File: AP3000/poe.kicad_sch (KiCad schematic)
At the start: 89 parts, among them IC2 TPS23751PWPR, J11 Barrel_Jack, Q1 BSC520N15NS3 G, Q2 MMBT2907ALT1G, Q3 MMBT3906LT1G, U10 SIR422DP-T1-GE3, U12 TCMT1107, U13 TLV431ACDBZR

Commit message: Route all the high speed lines and most gpio
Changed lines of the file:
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@@
   (junction (at 271.78 77.47) (diameter 1.016) (color 0 0 0 0))
   (junction (at 271.78 93.98) (diameter 1.016) (color 0 0 0 0))
+  (no_connect (at 125.73 155.575))
   (no_connect (at 115.57 155.575))
-  (no_connect (at 125.73 155.575))
   (no_connect (at 40.64 114.3))
   (wire (pts (xy 15.24 77.47) (xy 26.67 77.47))
@@
     (effects (font (size 1.27 1.27)) (justify right bottom))
   )
-  (label "+5V" (at 265.43 77.47 0)
+  (label "+5v" (at 265.43 77.47 0)
     (effects (font (size 1.27 1.27)) (justify left bottom))
   )
-  (label "+5V" (at 274.32 106.68 0)
+  (label "+5v" (at 274.32 106.68 0)
     (effects (font (size 1.27 1.27)) (justify left bottom))
   )

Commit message: AP3000: Fixup PartsBoxID linkage and placed first order Working on a design for a 5 GHz panel antenna array for a point-to-point replacement
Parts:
- C10, C9: PartsBoxID EEE-FK0J331XP -> EEEFK0J331XP
- C12, C13, C14: PartsBoxID 1206-100uF-X5R-6.3V -> 1206-47uF-X5R-10V
- C29: PartsBoxID EEE-FK1E220R -> EEEFK1E220R
- D17, D18: PartsBoxID (none) -> BAT54SW-7-F
- IC2: PartsBoxID (none) -> TPS23751PWPR
- Q1: PartsBoxID BSC520N15NS3 G -> BSC520N15NS3GATMA1
- U12: PartsBoxID (none) -> TCMT1107
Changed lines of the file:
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@@
       (effects (font (size 1.27 1.27)) hide)
     )
-    (property "PartsBoxID" "1206-100uF-X5R-6.3V" (id 4) (at 212.09 85.09 0)
+    (property "PartsBoxID" "1206-47uF-X5R-10V" (id 4) (at 212.09 85.09 0)
       (effects (font (size 1.27 1.27)) hide)
     )
@@
       (effects (font (size 1.27 1.27)) hide)
     )
-    (property "PartsBoxID" "1206-100uF-X5R-6.3V" (id 4) (at 220.98 85.09 0)
+    (property "PartsBoxID" "1206-47uF-X5R-10V" (id 4) (at 220.98 85.09 0)
       (effects (font (size 1.27 1.27)) hide)
     )
@@
       (effects (font (size 1.27 1.27)) hide)
     )
-    (property "PartsBoxID" "1206-100uF-X5R-6.3V" (id 4) (at 229.87 85.09 0)
+    (property "PartsBoxID" "1206-47uF-X5R-10V" (id 4) (at 229.87 85.09 0)
       (effects (font (size 1.27 1.27)) hide)
     )
@@
       (effects (font (size 1.27 1.27)) (justify left) hide)
     )
-    (property "PartsBoxID" "EEE-FK1E220R" (id 4) (at 116.84 104.14 0)
+    (property "PartsBoxID" "EEEFK1E220R" (id 4) (at 116.84 104.14 0)
       (effects (font (size 1.27 1.27)) hide)
     )
@@
       (effects (font (size 1.27 1.27)) (justify left) hide)
     )
-    (property "PartsBoxID" "EEE-FK0J331XP" (id 4) (at 238.76 78.74 0)
+    (property "PartsBoxID" "EEEFK0J331XP" (id 4) (at 238.76 78.74 0)
       (effects (font (size 1.27 1.27)) hide)
     )
@@
       (effects (font (size 1.27 1.27)) (justify left) hide)
     )
-    (property "PartsBoxID" "EEE-FK0J331XP" (id 4) (at 262.89 78.74 0)
+    (property "PartsBoxID" "EEEFK0J331XP" (id 4) (at 262.89 78.74 0)
       (effects (font (size 1.27 1.27)) hide)
     )
@@
       (effects (font (size 1.27 1.27)) hide)
     )
+    (property "PartsBoxID" "BAT54SW-7-F" (id 4) (at 186.69 137.16 0)
+      (effects (font (size 1.27 1.27)) hide)
+    )
   )
   (symbol (lib_id "Diode:BAT54S") (at 254.635 129.54 270) (mirror x) (unit 1)
@@
       (effects (font (size 1.27 1.27)) hide)
     )
+    (property "PartsBoxID" "BAT54SW-7-F" (id 4) (at 254.635 129.54 0)
+      (effects (font (size 1.27 1.27)) hide)
+    )
   )
   (symbol (lib_id "Isolator:TCMT1107") (at 214.63 139.7 0) (mirror y) (unit 1)
@@
       (effects (font (size 1.27 1.27)) (justify left) hide)
     )
+    (property "PartsBoxID" "TCMT1107" (id 4) (at 214.63 139.7 0)
+      (effects (font (size 1.27 1.27)) hide)
+    )
   )
   (symbol (lib_id "AP3000:TRANSF5") (at 120.65 155.575 180) (unit 1)
@@
       (effects (font (size 1.27 1.27)) (justify left) hide)
     )
-    (property "PartsBoxID" "BSC520N15NS3 G" (id 4) (at 144.78 113.03 0)
+    (property "PartsBoxID" "BSC520N15NS3GATMA1" (id 4) (at 144.78 113.03 0)
       (effects (font (size 1.27 1.27)) hide)
     )
@@
       (effects (font (size 1.27 1.27)) (justify left) hide)
     )
-  )
+    (property "PartsBoxID" "TPS23751PWPR" (id 4) (at 40.64 99.06 0)
+      (effects (font (size 1.27 1.27)) hide)
+    )
+  )

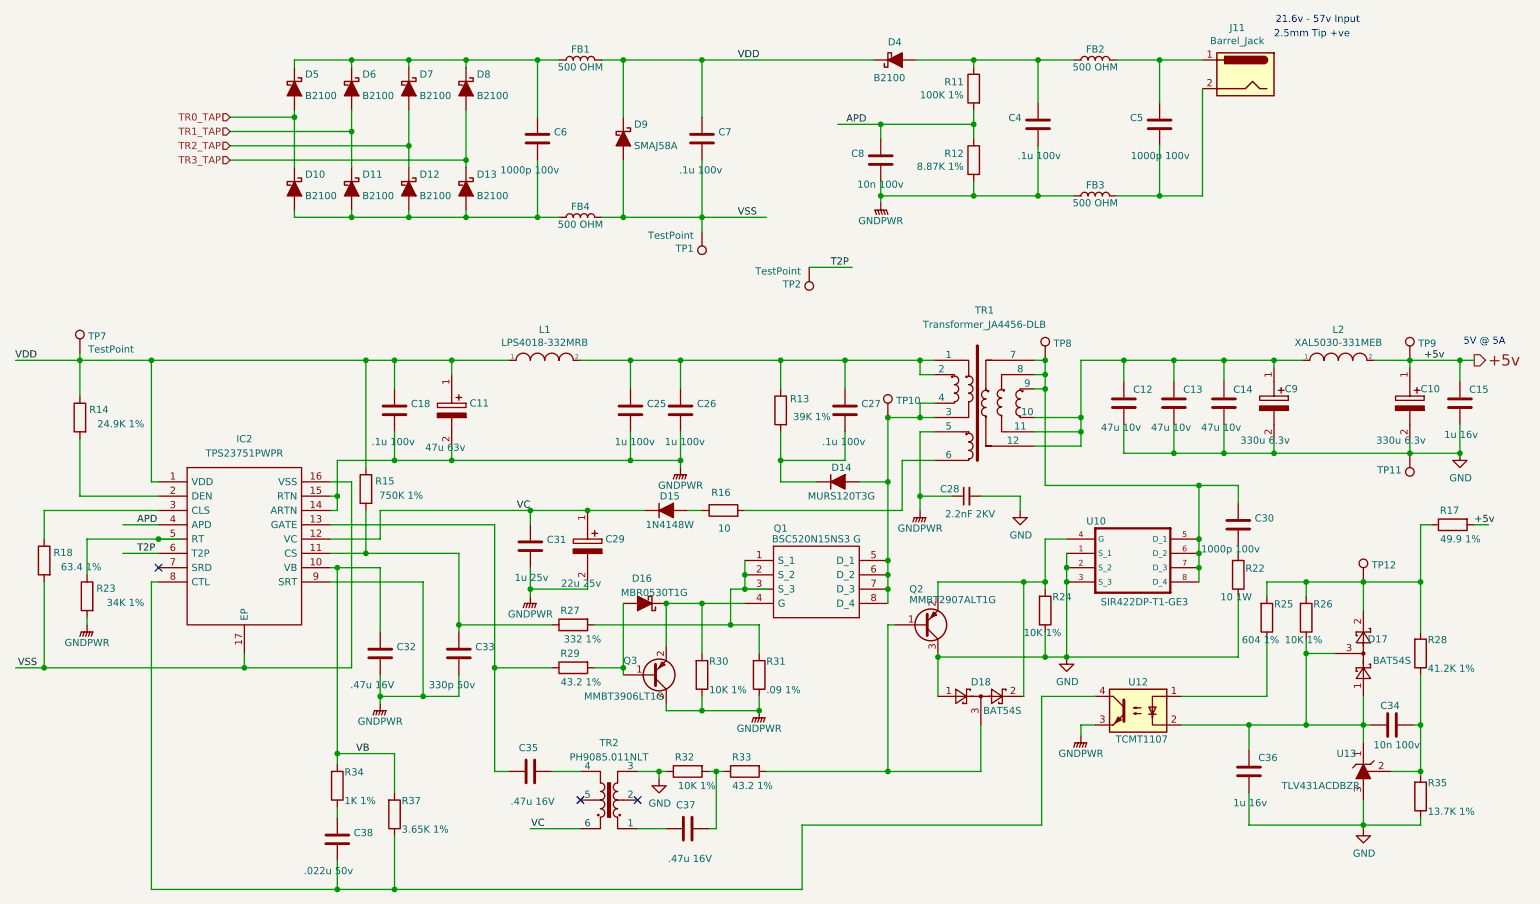
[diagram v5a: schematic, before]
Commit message: Rework AP3000 PoE section, power section and change solder paste to -10% overall, -15% for small chips / mpcie and -20% for the raspi connector
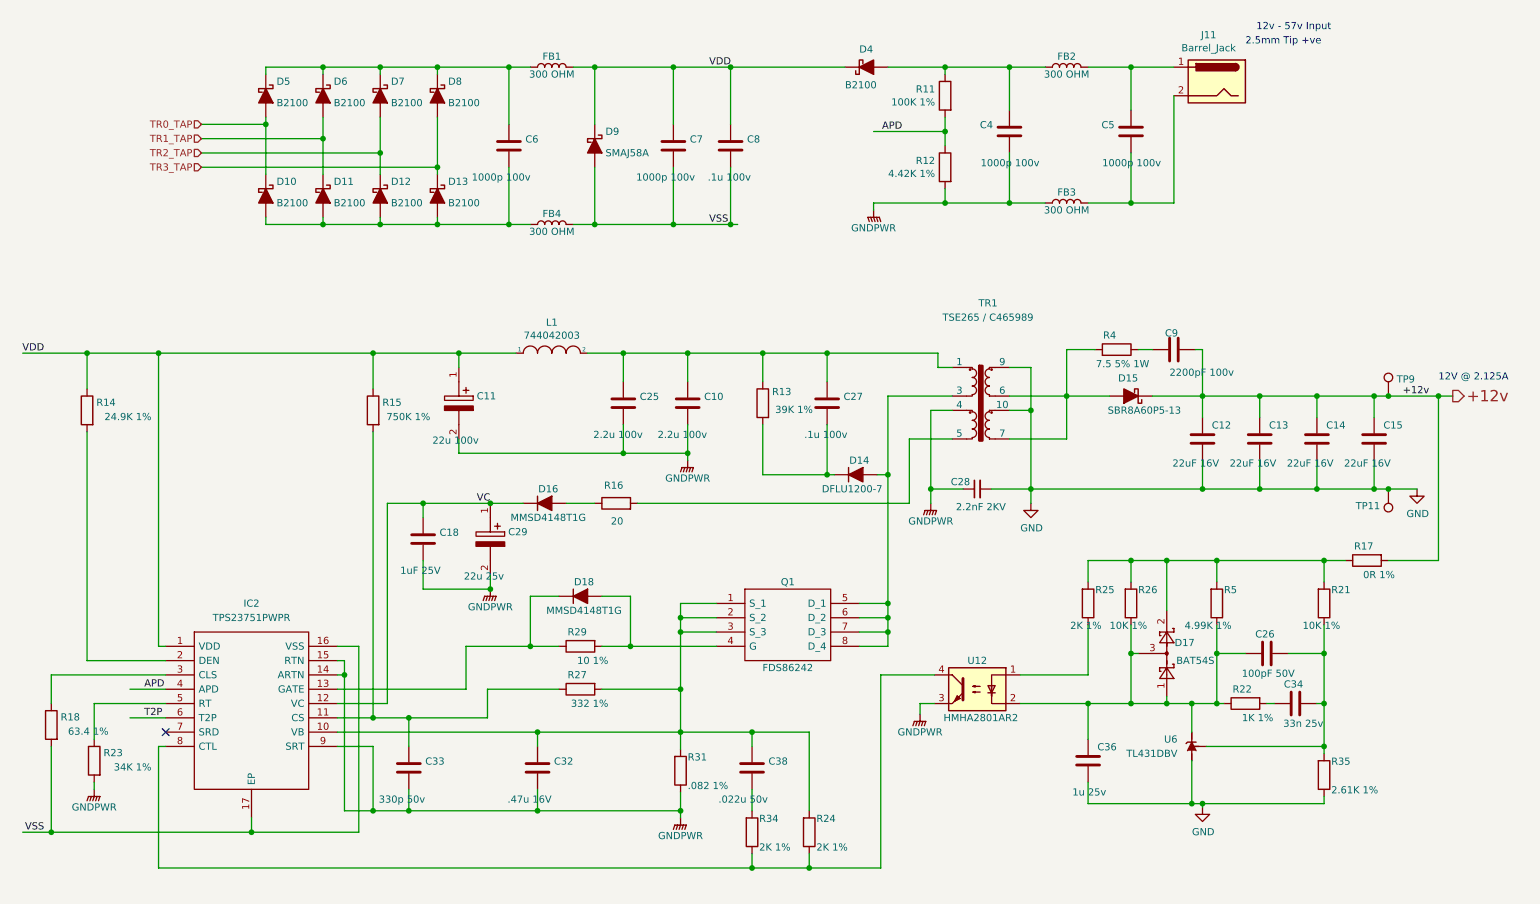
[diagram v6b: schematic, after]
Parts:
- removed C10, C9: 330u 6.3v, Capacitor_SMD:CP_Elec_6.3x7.7, symbol AP3000-rescue:EEEFK2A330P-EEEFK2A330P
- removed C30: 1000p 100v, Capacitor_SMD:C_0805_2012Metric, symbol Device:C
- removed C31: 1u 25v, Capacitor_SMD:C_0805_2012Metric, symbol Device:C
- removed C35, C37: .47u 16V, Capacitor_SMD:C_0603_1608Metric, symbol Device:C
- removed D15: 1N4148W, Diode_SMD:D_SOD-123, symbol Device:D_ALT
- removed D16: MBR0530T1G, Diode_SMD:D_SOD-123, symbol Device:D_Schottky_ALT
- removed D18: BAT54S, Package_TO_SOT_SMD:SOT-23, symbol Diode:BAT54S
- removed L2: XAL5030-331MEB, Inductor_SMD:L_Coilcraft_XAL5030, symbol pspice:INDUCTOR
- removed Q2: MMBT2907ALT1G, Package_TO_SOT_SMD:SOT-23, symbol Device:Q_PNP_BEC
- removed Q3: MMBT3906LT1G, Package_TO_SOT_SMD:SOT-23, symbol Device:Q_PNP_BEC
- removed R28: 41.2K 1%, Resistor_SMD:R_0402_1005Metric, symbol Device:R
- removed R30, R32: 10K 1%, Resistor_SMD:R_0402_1005Metric, symbol Device:R
- removed R33: 43.2 1%, Resistor_SMD:R_0402_1005Metric, symbol Device:R
- removed R37: 3.65K 1%, Resistor_SMD:R_0402_1005Metric, symbol Device:R
- removed TP1, TP10, TP12, TP2, TP7, TP8: TestPoint, TestPoint:TestPoint_Pad_2.0x2.0mm, symbol Connector:TestPoint
- removed TR2: PH9085.011NLT, AP3000:XFMR_PH9085.011NLT, symbol AP3000:TRANSF5
- removed U10: SIR422DP-T1-GE3, Scott:TRANS_STL60P4LLF6, symbol STL90N6F7:STL90N6F7
- removed U13: TLV431ACDBZR, Package_TO_SOT_SMD:SOT-23, symbol dk_PMIC-Voltage-Reference:TL431AIDBZR
- added C10: 2.2u 100v, Capacitor_SMD:C_1210_3225Metric, symbol Device:C
- added C9: 2200pF 100v, Capacitor_SMD:C_0603_1608Metric, symbol Device:C
- added D15: SBR8A60P5-13, Diode_SMD:D_PowerDI-5, symbol Device:D_Schottky_ALT
- added D16, D18: MMSD4148T1G, Diode_SMD:D_SOD-123, symbol Device:D_ALT
- added R21: 10K 1%, Resistor_SMD:R_0603_1608Metric, symbol Device:R
- added R4: 7.5 5% 1W, Resistor_SMD:R_2512_6332Metric, symbol Device:R
- added R5: 4.99K 1%, Resistor_SMD:R_0603_1608Metric, symbol Device:R
- added U6: TL431DBV, Package_TO_SOT_SMD:SOT-23-5, symbol Reference_Voltage:TL431DBV
- C11: value 47u 63v -> 22u 100v; PartsBoxID EEE-FK1J470P -> EEEFK2A220P
- C12, C13, C14: value 47u 10v -> 22uF 16V; footprint Capacitor_SMD:C_1206_3216Metric -> Capacitor_SMD:C_1210_3225Metric; Part Description 47uF 10% or 20% 10V Ceramic Capacitor X5R 1206 -> GCM32ER71C226KE19L; PartsBoxID 1206-47uF-X5R-10V -> 1210-22uF-X7R-16V
- C15: value 1u 16v -> 22uF 16V; footprint Capacitor_SMD:C_0805_2012Metric -> Capacitor_SMD:C_1210_3225Metric; Field4 (none) -> Mouser; Part Description 1uF 10% or 20% 16V Ceramic Capacitor X7R 0805 -> GCM32ER71C226KE19L; PartsBoxID 0805-1uF-X7R-16V -> 1210-22uF-X7R-16V
- C18: value .1u 100v -> 1uF 25V; footprint Capacitor_SMD:C_0603_1608Metric -> Capacitor_SMD:C_0805_2012Metric; Part Description .1uF 10% or 20% 100V Ceramic Capacitor X7R 0603 -> C2012X5R1E105K; PartsBoxID 0603-100nF-X7R-100V -> 0805-1uF-X5R-25V
- C25: value 1u 100v -> 2.2u 100v; footprint Capacitor_SMD:C_1206_3216Metric -> Capacitor_SMD:C_1210_3225Metric; Field7 CL31B105KCHNNNE -> (none); Part Description 1uF 10% or 20% 100V Ceramic Capacitor X7R 1206 -> (none); PartsBoxID 1206-1uF-X7R-100V -> 1210-2.2uF-X7R-100V
- C26: value 1u 100v -> 100pF 50V; footprint Capacitor_SMD:C_1206_3216Metric -> Capacitor_SMD:C_0603_1608Metric; Field7 CL31B105KCHNNNE -> (none); Part Description 1uF 10% or 20% 100V Ceramic Capacitor X7R 1206 -> (none); PartsBoxID 1206-1uF-X7R-100V -> GRM1885C1H101JA01D
- C34: value 10n 100v -> 33n 25v; Part Description .01uF 10% or 20% 100V Ceramic Capacitor X7R 0603 -> (none); PartsBoxID 0603-10nF-X7R-100V -> 0603-33nF-X7R-25V
- C36: value 1u 16v -> 1u 25v; Part Description 1uF 10% or 20% 16V Ceramic Capacitor X7R 0805 -> (none); PartsBoxID 0805-1uF-X7R-16V -> 0805-1uF-X7R-25V
- C4, C7: value .1u 100v -> 1000p 100v; footprint Capacitor_SMD:C_0603_1608Metric -> Capacitor_SMD:C_0805_2012Metric; Field4 (none) -> Digikey; Field6 (none) -> CL21B102KCANNNC; Field7 (none) -> Samsung Electro-Mechanics; Part Description .1uF 10% or 20% 100V Ceramic Capacitor X7R 0603 -> 1000pF 10% or 20% 100V Ceramic Capacitor X7R 0805; PartsBoxID 0603-100nF-X7R-100V -> 0805-1000pF-X7R-100V
- C8: value 10n 100v -> .1u 100v; Part Description .01uF 10% or 20% 100V Ceramic Capacitor X7R 0603 -> .1uF 10% or 20% 100V Ceramic Capacitor X7R 0603; PartsBoxID 0603-10nF-X7R-100V -> 0603-100nF-X7R-100V
- D14: value MURS120T3G -> DFLU1200-7; footprint Diode_SMD:D_SMB -> Diode_SMD:D_PowerDI-123; PartsBoxID MURS120T3G -> DFLU1200-7
- FB1: value 500 OHM -> 300 OHM; footprint Inductor_SMD:L_1206_3216Metric -> Inductor_SMD:L_0603_1608Metric; PartsBoxID MI1206L501R-10 -> 742792641
- FB2, FB3, FB4: value 500 OHM -> 300 OHM; footprint Inductor_SMD:L_1206_3216Metric -> Inductor_SMD:L_0603_1608Metric
- IC2: footprint SOP65P640X120-17N -> Scott:HTSSOP-16-1EP_4.4x5mm_P0.65mm_EP3.4x5mm_Mask2.46x2.31mm_ThermalVias
- L1: value LPS4018-332MRB -> 744042003; footprint Inductor_SMD:L_Coilcraft_LPS4018 -> Scott:WE-TPC_4818_482892-744042003; Field7 Coilcraft -> (none); Part Description Fixed Inductors 3.3uH SMD 4018 -> (none); PartsBoxID LPS4018-332MRB -> 744042003
- Q1: value BSC520N15NS3 G -> FDS86242; footprint Scott:TRANS_BSC100N06LS3GATMA1 -> Package_SO:SO-8_3.9x4.9mm_P1.27mm; Arrow Part Number BSC190N15NS3GATMA1 -> (none); Arrow Price/Stock https://www.arrow.com/en/products/bsc190n15ns3gatma1/infine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 -> (none); Manufacturer_Name Infineon -> (none); Manufacturer_Part_Number BSC190N15NS3GATMA1 -> (none); Mouser Part Number 726-BSC190N15NS3GATM -> (none); Mouser Price/Stock https://www.mouser.co.uk/ProductDetail/Infineon-Technologie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 -> (none); PartsBoxID BSC520N15NS3GATMA1 -> FDS86242
- R11: footprint Resistor_SMD:R_0402_1005Metric -> Resistor_SMD:R_0603_1608Metric; PartsBoxID 0402-100K-1% -> 0603-100K-1%
- R12: value 8.87K 1% -> 4.42K 1%; footprint Resistor_SMD:R_0402_1005Metric -> Resistor_SMD:R_0603_1608Metric; Part Description Resistor 8.87K 0402 1% 63mW -> (none); PartsBoxID 0402-8.87K-1% -> 0603-4.42K-1%
- R15: footprint Resistor_SMD:R_0402_1005Metric -> Resistor_SMD:R_0603_1608Metric; PartsBoxID 0402-750K-1% -> 0603-750K-1%
- R16: value 10 -> 20; PartsBoxID 0805-10R-1% -> CRCW080520R0JNEA
- R17: value 49.9 1% -> 0R 1%; footprint Resistor_SMD:R_0402_1005Metric -> Resistor_SMD:R_0603_1608Metric; PartsBoxID 0402-49.9-1% -> 0603-0R-1%
- R18: footprint Resistor_SMD:R_0402_1005Metric -> Resistor_SMD:R_0603_1608Metric; PartsBoxID 0402-63.4-1%-100mW -> 0603-63.4-1%-100mW
- R22: value 10 1W -> 1K 1%; footprint Resistor_SMD:R_2512_6332Metric -> Resistor_SMD:R_0603_1608Metric; Part Description Resistor 10 2512 5% 1W -> (none); PartsBoxID 2512-10R-5%-1W -> 0603-1K-1%
- R23: footprint Resistor_SMD:R_0402_1005Metric -> Resistor_SMD:R_0603_1608Metric; PartsBoxID 0402-34K-1% -> 0603-34K-1%
- R24: value 10K 1% -> 2K 1%; footprint Resistor_SMD:R_0402_1005Metric -> Resistor_SMD:R_0603_1608Metric; Part Description Resistor 10K 0402 1% 63mW -> (none); PartsBoxID 0402-10K-1% -> 0603-2K-1%
- R25: value 604 1% -> 2K 1%; footprint Resistor_SMD:R_0402_1005Metric -> Resistor_SMD:R_0603_1608Metric; Part Description Resistor 604 0402 1% 63mW -> (none); PartsBoxID 0402-604-1% -> 0603-2K-1%
- R26: footprint Resistor_SMD:R_0402_1005Metric -> Resistor_SMD:R_0603_1608Metric; PartsBoxID 0402-10K-1% -> 0603-10K-1%
- R27: footprint Resistor_SMD:R_0402_1005Metric -> Resistor_SMD:R_0603_1608Metric; PartsBoxID 0402-332-1% -> 0603-332-1%
- R29: value 43.2 1% -> 10 1%; footprint Resistor_SMD:R_0402_1005Metric -> Resistor_SMD:R_0603_1608Metric; PartsBoxID 0402-43.2-1% -> CRCW060310R0JNEA
- R31: value .09 1% -> .082 1%; footprint Resistor_SMD:R_0805_2012Metric -> Resistor_SMD:R_1206_3216Metric; Part Description Resistor .09 0805 1% 500mW -> (none); PartsBoxID 580060720008 -> RL1206FR-070R082L
- R34: value 1K 1% -> 2K 1%; footprint Resistor_SMD:R_0402_1005Metric -> Resistor_SMD:R_0603_1608Metric; Part Description Resistor 1K 0402 1% 63mW -> (none); PartsBoxID 0402-1K-1% -> 0603-2K-1%
- R35: value 13.7K 1% -> 2.61K 1%; footprint Resistor_SMD:R_0402_1005Metric -> Resistor_SMD:R_0603_1608Metric; Part Description Resistor 13.7K 0402 1% 63mW -> (none); PartsBoxID 0402-13.7K-1% -> 0603-2.61K-1%
- TP11, TP9: footprint TestPoint:TestPoint_Pad_2.0x2.0mm -> TestPoint:TestPoint_Keystone_5000-5004_Miniature; PartsBoxID (none) -> 5001
- TR1: value Transformer_JA4456-DLB -> TSE265 / C465989; footprint AP3000:SOP300P3000X1270-12N -> Scott:Transformer_TNK_TSE265; symbol AP3000:Transformer_JA4456-DLB -> Scott:Transformer_TNK_TSE265; PartsBoxID JA4456-DLB -> TSE265
- U12: value TCMT1107 -> HMHA2801AR2; PartsBoxID TCMT1107 -> HMHA2801AR2
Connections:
- net +5v is gone; now on net +12v: C15.1, R17.2, TP9.1
- net APD: no longer C8.1
- net GND: now also TR1.10, TR1.9, U6.5 (A); no longer R22.1, R24.1
- net GNDPWR: now also TR1.4, C10.2; no longer C26.2, C8.2, TR1.5
- net VC: now also C18.1, D16.1 (K)
- net VDD: now also C8.1; no longer C18.1
- net VSS: now also C8.2
- net at R24.2: now also C32.1, C38.1, IC2.10 (VB), Q1.1 (S_1), Q1.2 (S_2), Q1.3 (S_3), R27.2, R31.2
- net at R22.2: now also C34.1
- net +12v: now reaches C12.1, C13.1, C14.1
- net +12v: now also C9.2, D15.1 (K); no longer TR1.10, TR1.11, TR1.12
- net at R34.1: now also IC2.8 (CTL), R24.1, U12.4; no longer C38.1
- net at C36.1, D17.1, D17.3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: now also C26.1, R22.1, R5.1, U6.3 (K); no longer C34.1
- net at C34.2, R35.2: now also C26.2, R21.1, U6.4 (REF)
- net at Q1.4 (G): now also R29.2, D18.2 (A)
- net at D14.2 (A), Q1.5 (D_1), Q1.6 (D_2)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: no longer TR1.4
- net at D17.2, R17.1, R25.2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: now also R21.2, R5.2
- net at C25.1, C27.1, L1.2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: now also C10.1; no longer C26.1, TR1.2
- net at R16.2: now also TR1.5; no longer TR1.6
- net at IC2.13 (GATE), R29.1: now also D18.1 (K)
- net at R16.1: now also D16.2 (A)
- removed net VB: C32.1, IC2.10 (VB), R34.2
- new net: C38.2, R34.2
- new net: D15.2 (A), R4.2, TR1.6, TR1.7
- new net: C9.1, R4.1
- no-connect marks 3 -> 1
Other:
- note added: "12V @ 2.125A"
- note added: "12v - 57v Input"
- note removed: "21.6v - 57v Input"
- note removed: "5V @ 5A"
- moved on the sheet: C11, C12, C25, C27, C28, C29, C32, C33, C34, C36, C38, C5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

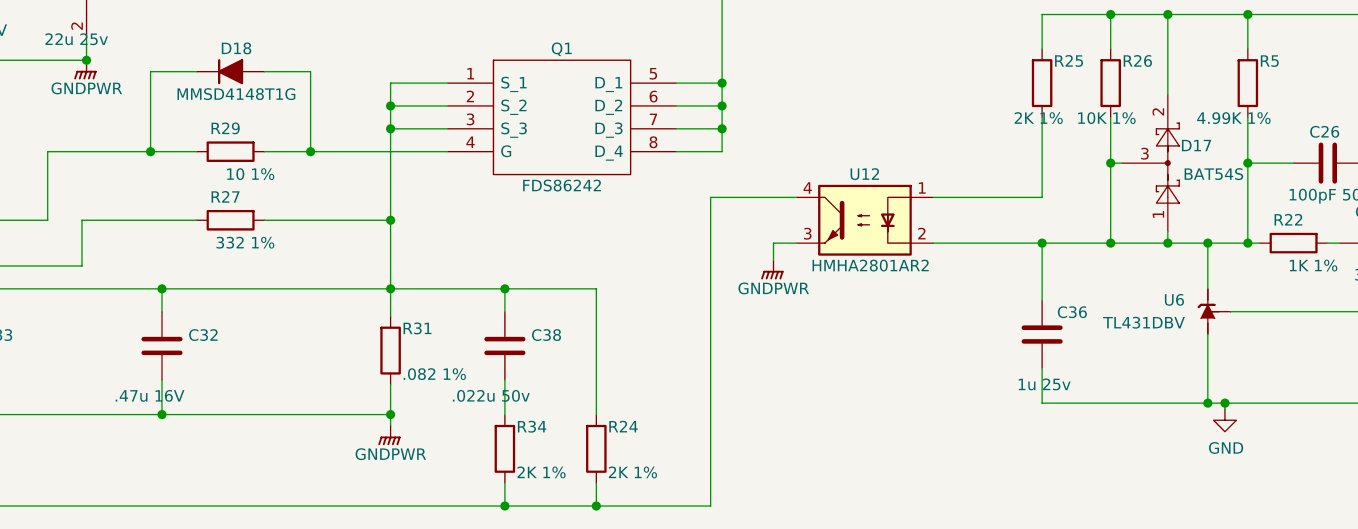
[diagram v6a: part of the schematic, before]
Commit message: Ordered AP3000 PCBs Ordered FlatAntPanel4x4 PCBs Ordered FlatAntPanel4x4_Reflector PCBs
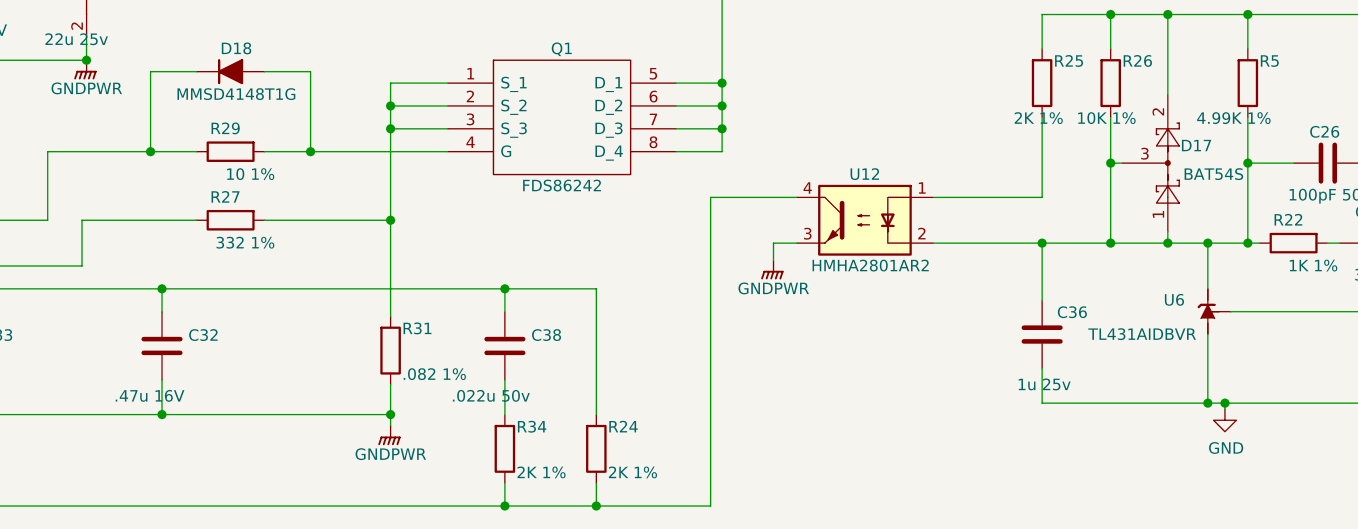
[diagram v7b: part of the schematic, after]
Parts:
- C11: PartsBoxID EEEFK2A220P -> EEE-FK2A220P
- C9: PartsBoxID C1608X7R2A222K -> 0603-2200pF-X7R-100V
- FB2, FB3, FB4: PartsBoxID MI1206L501R-10 -> 742792641
- R31: PartsBoxID RL1206FR-070R082L -> KDV12FR082ET
- U6: value TL431DBV -> TL431AIDBVR; PartsBoxID (none) -> TL431AIDBVR
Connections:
- net at Q1.1 (S_1), Q1.2 (S_2), Q1.3 (S_3)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: no longer C32.1, C38.1, IC2.10 (VB), R24.2
- new net: C32.1, C38.1, IC2.10 (VB), R24.2
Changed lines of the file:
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@@
   (junction (at 133.35 125.73) (diameter 1.016) (color 0 0 0 0))
   (junction (at 133.35 135.89) (diameter 1.016) (color 0 0 0 0))
-  (junction (at 133.35 143.51) (diameter 1.016) (color 0 0 0 0))
   (junction (at 133.35 157.48) (diameter 1.016) (color 0 0 0 0))
   (junction (at 134.62 76.2) (diameter 1.016) (color 0 0 0 0))
@@
     (stroke (width 0) (type solid) (color 0 0 0 0))
   )
-  (wire (pts (xy 107.95 143.51) (xy 133.35 143.51))
+  (wire (pts (xy 107.95 143.51) (xy 146.05 143.51))
     (stroke (width 0) (type solid) (color 0 0 0 0))
   )
@@
     (stroke (width 0) (type solid) (color 0 0 0 0))
   )
-  (wire (pts (xy 133.35 135.89) (xy 133.35 143.51))
-    (stroke (width 0) (type solid) (color 0 0 0 0))
-  )
-  (wire (pts (xy 133.35 143.51) (xy 133.35 146.558))
+  (wire (pts (xy 133.35 135.89) (xy 133.35 146.558))
     (stroke (width 0) (type solid) (color 0 0 0 0))
   )
@@
     (stroke (width 0) (type solid) (color 0 0 0 0))
   )
-  (wire (pts (xy 146.05 143.51) (xy 133.35 143.51))
-    (stroke (width 0) (type solid) (color 0 0 0 0))
-  )
   (wire (pts (xy 146.05 146.05) (xy 146.05 143.51))
     (stroke (width 0) (type solid) (color 0 0 0 0))
@@
       (effects (font (size 1.27 1.27)) hide)
     )
-    (property "PartsBoxID" "MI1206L501R-10" (id 4) (at 110.49 53.34 0)
+    (property "PartsBoxID" "742792641" (id 4) (at 110.49 53.34 0)
       (effects (font (size 1.27 1.27)) hide)
     )
@@
       (effects (font (size 1.27 1.27)) hide)
     )
-    (property "PartsBoxID" "MI1206L501R-10" (id 4) (at 201.93 25.4 0)
+    (property "PartsBoxID" "742792641" (id 4) (at 201.93 25.4 0)
       (effects (font (size 1.27 1.27)) hide)
     )
@@
       (effects (font (size 1.27 1.27)) hide)
     )
-    (property "PartsBoxID" "MI1206L501R-10" (id 4) (at 201.93 49.53 0)
+    (property "PartsBoxID" "742792641" (id 4) (at 201.93 49.53 0)
       (effects (font (size 1.27 1.27)) hide)
     )
@@
       (effects (font (size 1.27 1.27)) hide)
     )
-    (property "PartsBoxID" "RL1206FR-070R082L" (id 4) (at 133.35 150.368 0)
+    (property "PartsBoxID" "KDV12FR082ET" (id 4) (at 133.35 150.368 0)
       (effects (font (size 1.27 1.27)) hide)
     )
@@
       (effects (font (size 1.27 1.27)) (justify right))
     )
-    (property "Value" "TL431DBV" (id 1) (at 221.615 147.32 90)
+    (property "Value" "TL431AIDBVR" (id 1) (at 222.885 148.59 90)
       (effects (font (size 1.27 1.27)) (justify right))
     )
@@
       (effects (font (size 1.27 1.27) italic) hide)
     )
+    (property "PartsBoxID" "TL431AIDBVR" (id 4) (at 224.155 146.05 0)
+      (effects (font (size 1.27 1.27)) hide)
+    )
   )
   (symbol (lib_id "Device:C") (at 85.09 149.86 0) (unit 1)
@@
       (effects (font (size 1.27 1.27)) hide)
     )
-    (property "PartsBoxID" "C1608X7R2A222K" (id 4) (at 220.98 75.565 0)
+    (property "PartsBoxID" "0603-2200pF-X7R-100V" (id 4) (at 220.98 75.565 0)
       (effects (font (size 1.27 1.27)) hide)
     )
@@
       (effects (font (size 1.27 1.27)) (justify left) hide)
     )
-    (property "PartsBoxID" "EEEFK2A220P" (id 4) (at 93.98 78.74 0)
+    (property "PartsBoxID" "EEE-FK2A220P" (id 4) (at 93.98 78.74 0)
       (effects (font (size 1.27 1.27)) hide)
     )
